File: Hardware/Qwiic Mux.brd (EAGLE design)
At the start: 35.6 x 54.6 mm, 88 parts, among them J2 SMD, J3 SMD, U2 PCA9548A

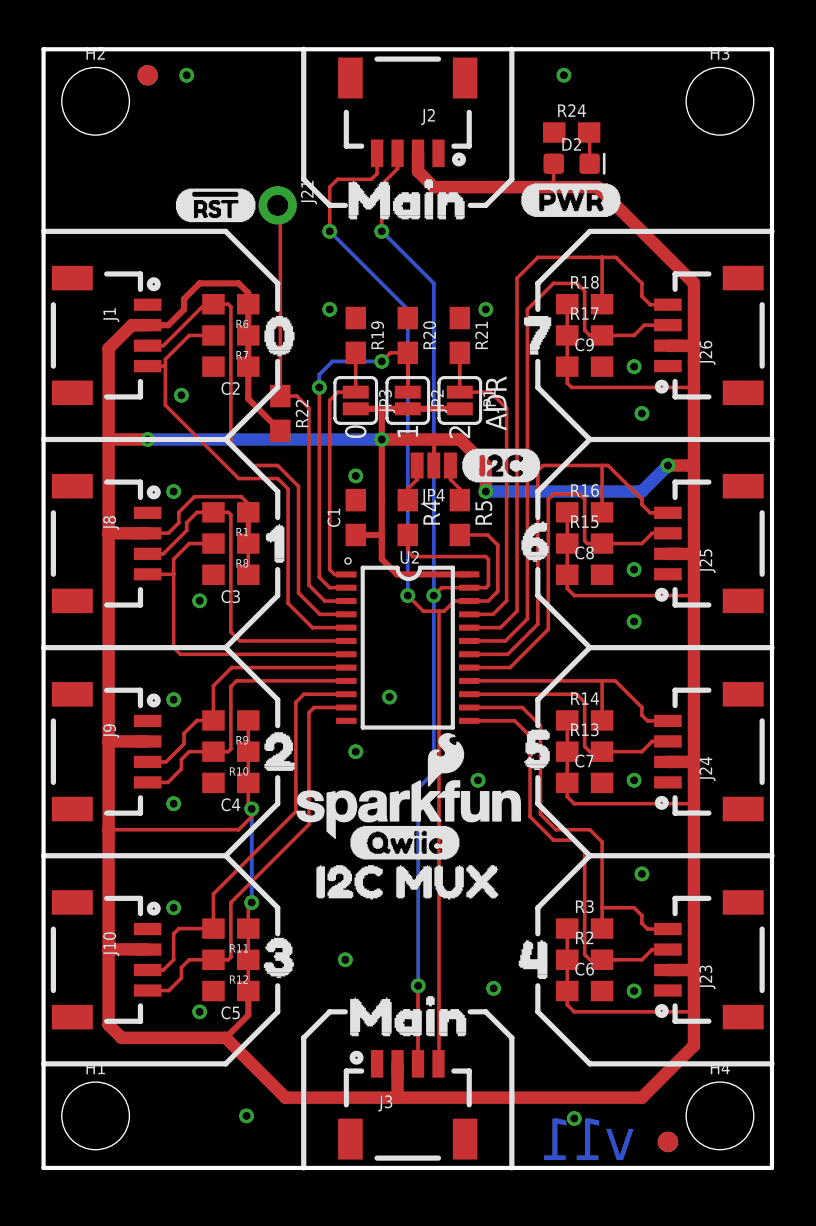
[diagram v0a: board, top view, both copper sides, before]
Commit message: Update Qwiic label. Update labels on ADR and RESET pins.
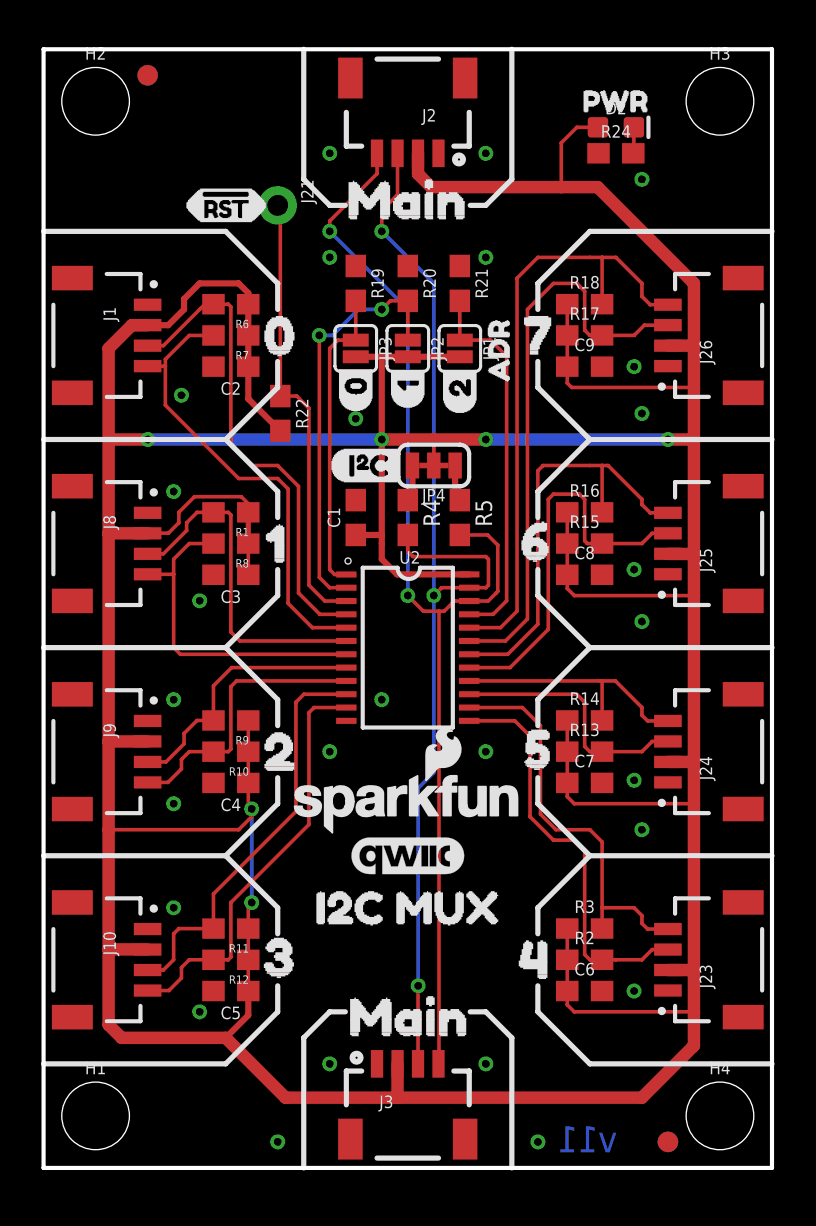
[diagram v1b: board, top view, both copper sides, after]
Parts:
- added U$31: (no value), SparkFun-Buzzard:PWR_TO
- added U$32: (no value), buzzard_labels (13):15
- added U$33: (no value), buzzard_labels (13):26
- added U$34: (no value), buzzard_labels (13):ADR3
- added U$35: (no value), buzzard_labels (14):I#C6
- added U$36: (no value), SparkFun-Aesthetics:QWIIC_5.5MM
- J1, J10, J23, J24, J25, J26, J8, J9: value (none) -> QWIIC_RIGHT_ANGLE; device SparkFun-Connectors:1X04_1MM_RA -> SparkFun-Connectors:JST04_1MM_RA
- JP1, JP2, JP3: value (none) -> JUMPER-SMT_2_NO_SILK
- JP4: value JUMPER-SMT_3_2-NC_PASTE_NO-SILK -> JUMPER-SMT_3_2-NC_TRACE_SILK; device SparkFun-Jumpers:SMT-JUMPER_3_2-NC_PASTE_NO-SILK -> SparkFun-Jumpers:SMT-JUMPER_3_2-NC_TRACE_SILK
- U$14, U$26: device buzzard_labels (10):#RST10 -> SparkFun-Buzzard:!RST_I
- U$3: device Labels-0_04:(PWR) -> buzzard_labels (10):I2C_MUX8
- U$4: device Labels-0_04:(QWIIC) -> SparkFun-Aesthetics:QWIIC_5.5MM
- U$5: device Labels-0_04:(I2C) -> buzzard_labels (13):04
- moved U$3 34.5 mm to (23.6, 12.7), flipped to the bottom
- moved U$2 9.81 mm to (17.8, 17.8)
- moved U$1 6.11 mm to (17.8, 17.8)
- moved U$5 5.68 mm to (15.2, 36.8), turned to 90 degrees
- moved U$4 2.99 mm to (17.8, 15.2)
- moved D2 2.80 mm to (27.9, 50.8)
- moved JP1 2.54 mm to (20.3, 40.0)
- moved JP2 2.54 mm to (17.8, 40.0)
- moved JP3 2.54 mm to (15.2, 40.0)
- moved R19 2.54 mm to (15.2, 43.2)
- moved R20 2.54 mm to (17.8, 43.2)
- moved R21 2.54 mm to (20.3, 43.2)
- moved R24 2.39 mm to (27.9, 49.5)
- moved U$15 1.27 mm to (11.9, 12.7)
- moved U$14 0.51 mm to (6.73, 47.0)
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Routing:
- net 3.3V: track 272.4 -> 275.0 mm
- net ADR2: track 16.0 -> 18.6 mm
- net ADR0: track 12.5 -> 15.1 mm
- net ADR1: track 18.1 -> 20.3 mm
- net MAIN_SCL: track 56.6 -> 55.7 mm
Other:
- board text removed: "0"
- board text removed: "1"
- board text removed: "2"
- board text removed: "ADR"
